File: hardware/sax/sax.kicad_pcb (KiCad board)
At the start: 4 copper layers, 80 x 34.5 mm, 105 parts, among them IC1401 MP3V5004GP, J101 Cortex, J102 DX07S016JA3, J1101 NE8FAH, J1301 2x05_Horizontal, SW101 SKSG, SW102 SKSG, U101 TPS78433QWDRBRQ1, U102 ATSAMD51J, U1101 THVD2442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

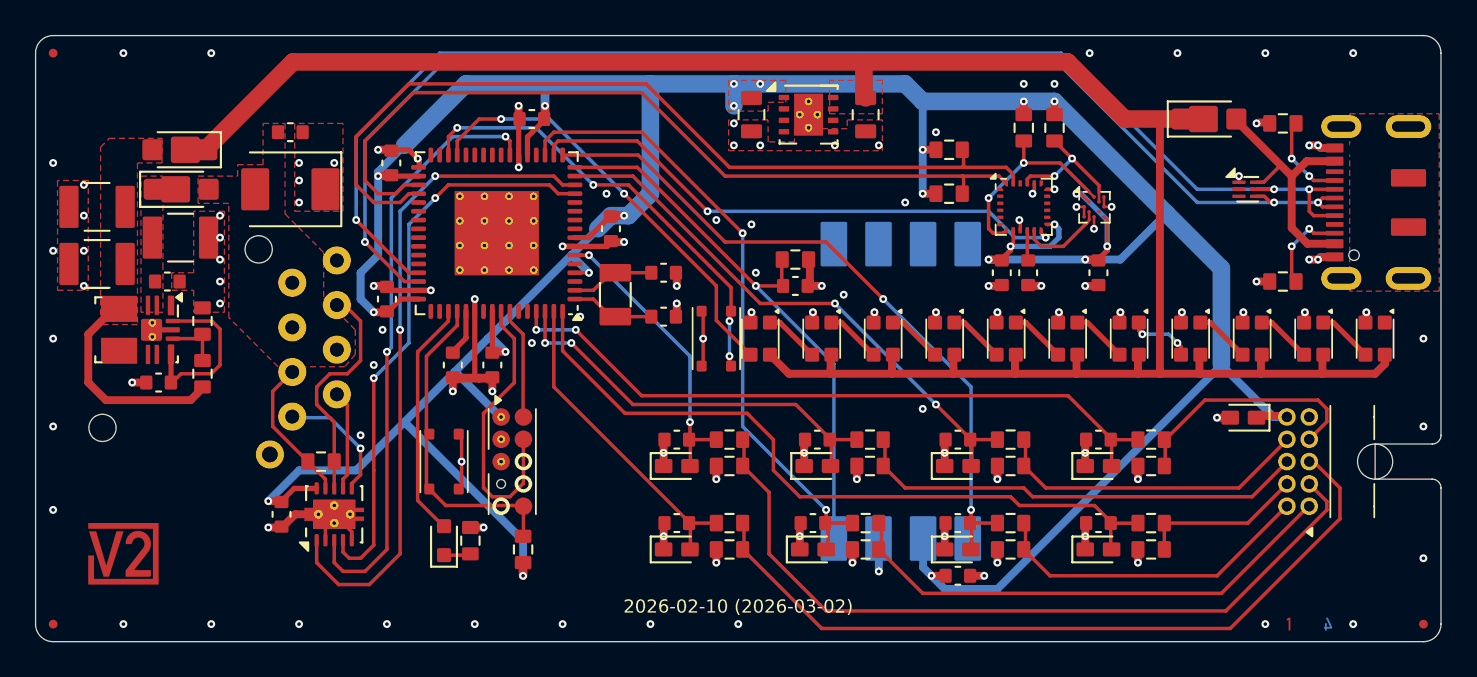
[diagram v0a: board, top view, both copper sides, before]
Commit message: Update ESD suppressor
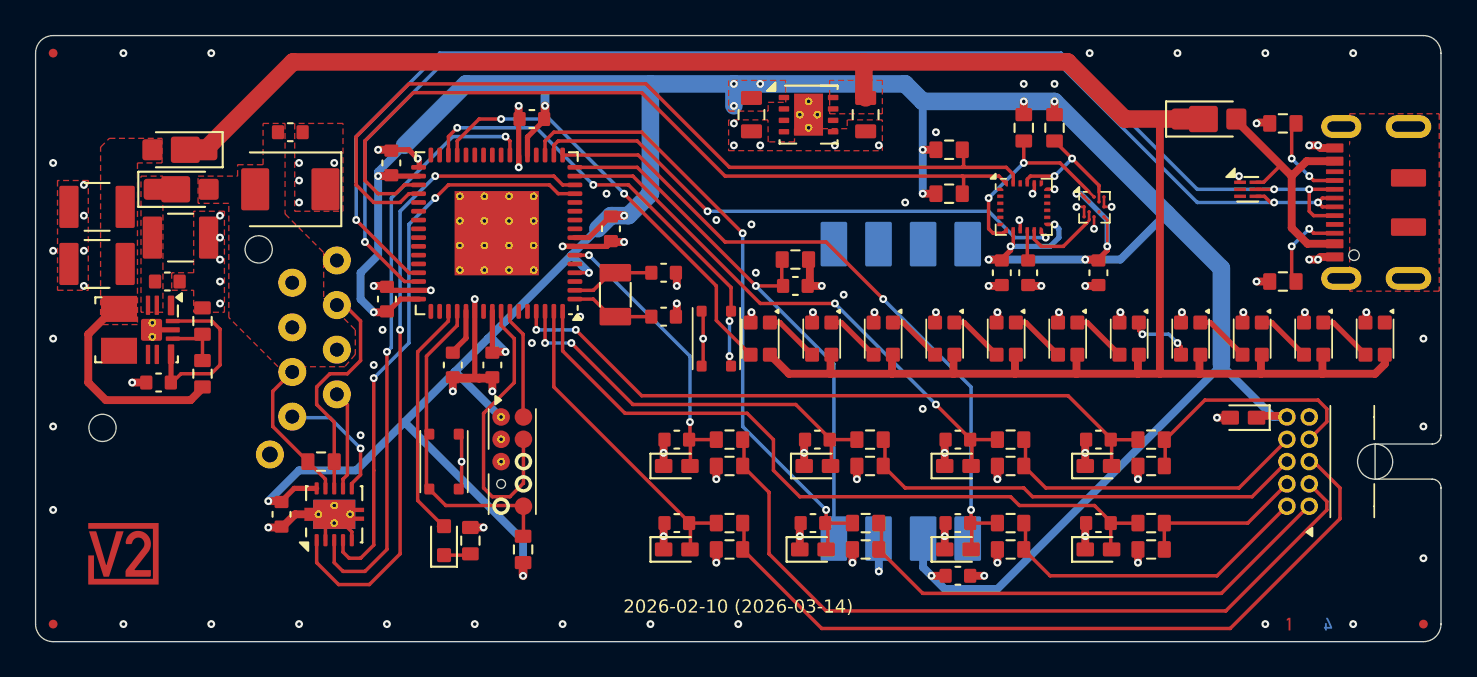
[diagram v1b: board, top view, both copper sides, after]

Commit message: KiCad 10
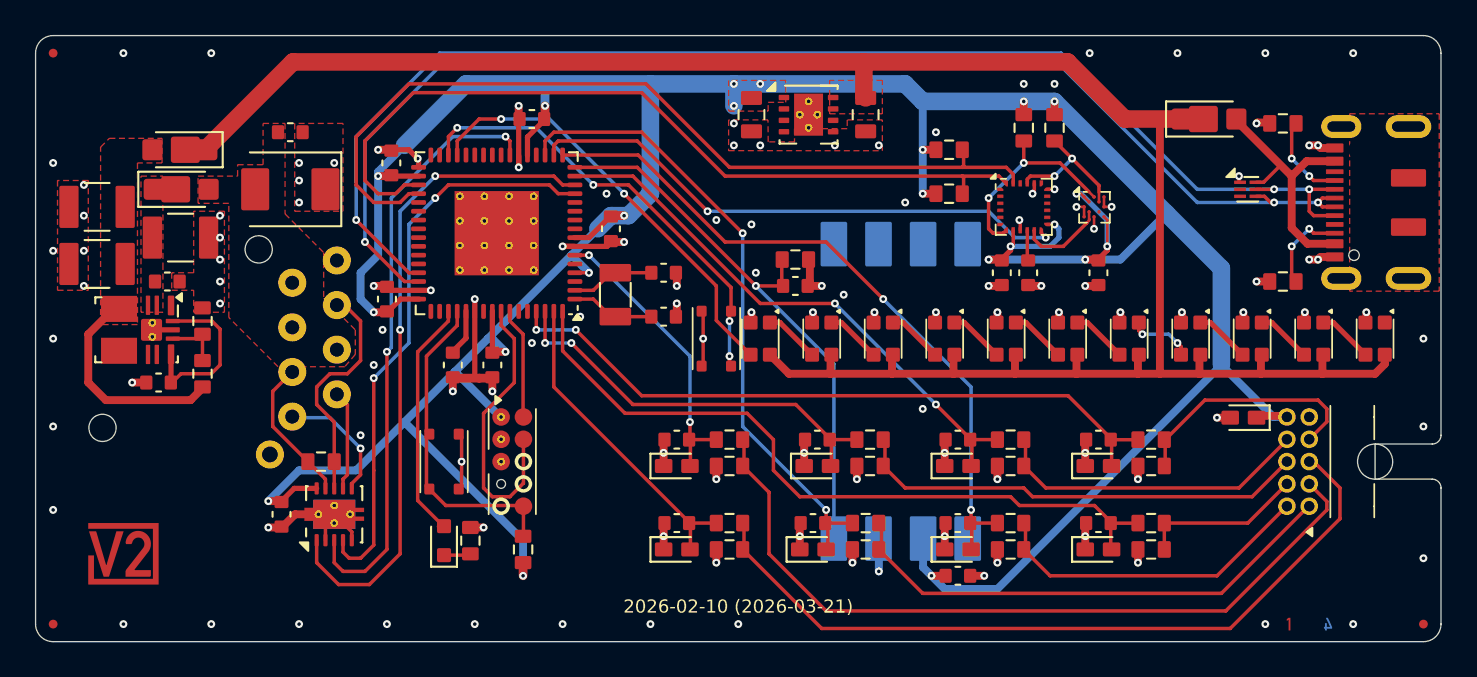
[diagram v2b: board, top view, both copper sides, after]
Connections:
- net /Orientation Sensor/Aux-SCK renamed /Orientation Sensor/Aux-SCL

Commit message: Refresh
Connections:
- net +VBUS renamed /+VBUS
- net +VLINK renamed /+VLINK
- net /VDDCORE renamed /+VDDCORE
- net Shield renamed /Shield
